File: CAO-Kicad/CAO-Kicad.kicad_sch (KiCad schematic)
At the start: 3 parts, among them J1 Conn_01x02

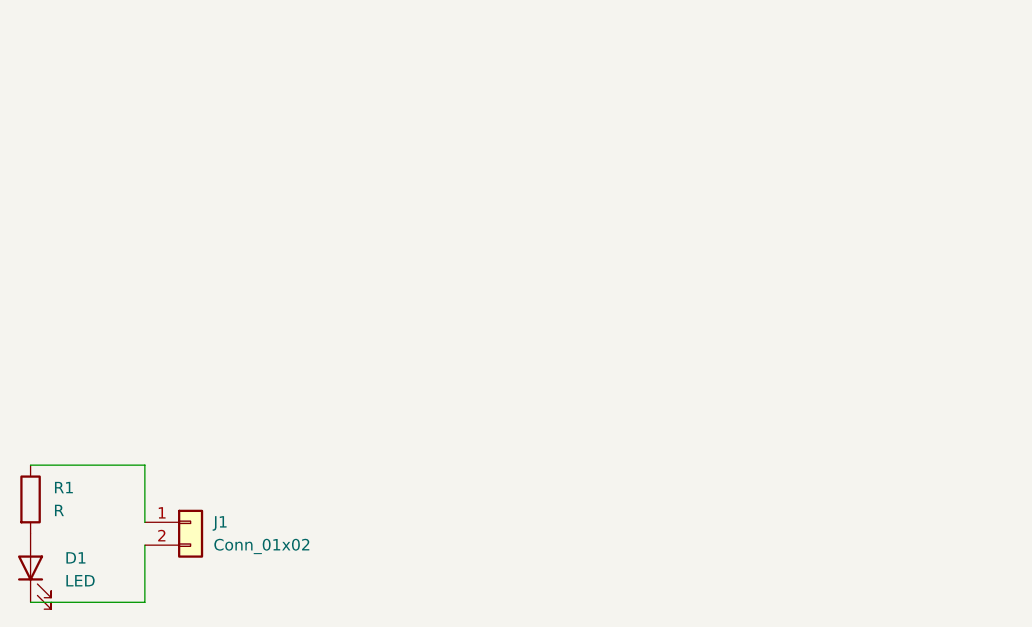
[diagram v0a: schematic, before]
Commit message: Ajout du conn ICSP et du contour de carte 100x100mm
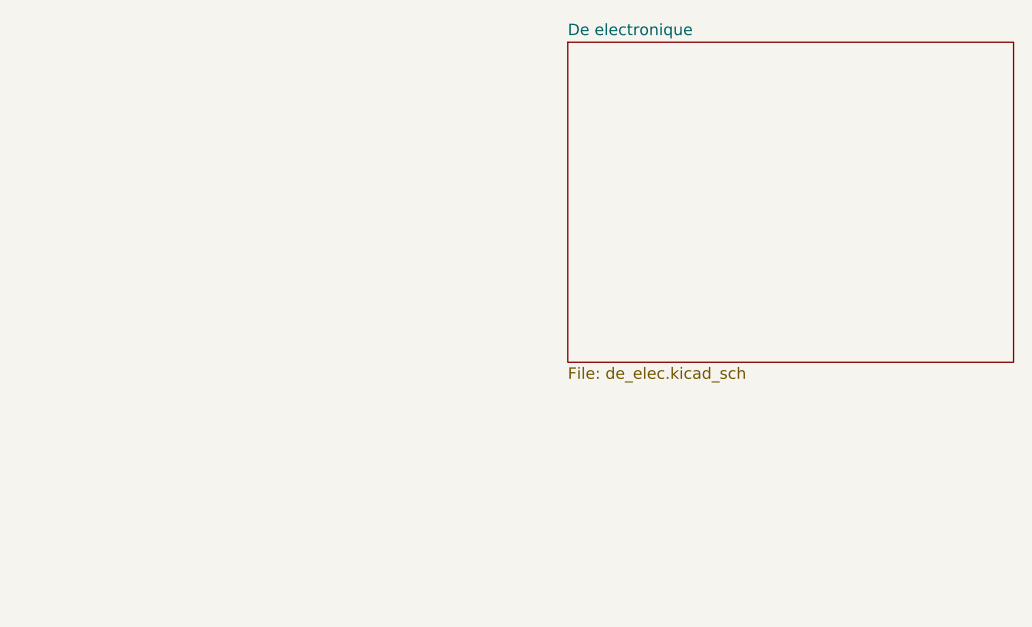
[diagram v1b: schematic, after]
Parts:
- removed D1: LED, LED_THT:LED_D5.0mm, symbol Device:LED
- removed J1: Conn_01x02, Connector_PinHeader_2.54mm:PinHeader_1x02_P2.54mm_Vertical, symbol Connector_Generic:Conn_01x02
- removed R1: R, Resistor_THT:R_Axial_DIN0207_L6.3mm_D2.5mm_P10.16mm_Horizontal, symbol Device:R
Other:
- added sheet De electronique (de_elec.kicad_sch)
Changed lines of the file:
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@@
     (rev "1.0")
   )
-  (wire (pts (xy 78.74 74.93) (xy 91.44 74.93))
-    (stroke (width 0) (type solid) (color 0 0 0 0))
-  )
-  (wire (pts (xy 78.74 90.17) (xy 91.44 90.17))
-    (stroke (width 0) (type solid) (color 0 0 0 0))
-  )
-  (wire (pts (xy 91.44 81.28) (xy 91.44 74.93))
-    (stroke (width 0) (type solid) (color 0 0 0 0))
-  )
-  (wire (pts (xy 91.44 83.82) (xy 91.44 90.17))
-    (stroke (width 0) (type solid) (color 0 0 0 0))
-  )
-  (symbol (lib_id "Device:R") (at 78.74 78.74 0) (unit 1)
-    (in_bom yes) (on_board yes) (fields_autoplaced)
-    (property "Reference" "R1" (id 0) (at 81.28 77.4699 0)
-      (effects (font (size 1.27 1.27)) (justify left))
+  (sheet (at 138.43 27.94) (size 49.53 35.56) (fields_autoplaced)
+    (stroke (width 0.0006) (type solid) (color 0 0 0 0))
+    (fill (color 0 0 0 0.0000))
+    (property "Nom feuille" "De electronique" (id 0) (at 138.43 27.3043 0)
+      (effects (font (size 1.27 1.27)) (justify left bottom))
     )
-    (property "Value" "R" (id 1) (at 81.28 80.0099 0)
-      (effects (font (size 1.27 1.27)) (justify left))
+    (property "Fichier de feuille" "de_elec.kicad_sch" (id 1) (at 138.43 64.0087 0)
+      (effects (font (size 1.27 1.27)) (justify left top))
     )
-    (property "Footprint" "Resistor_THT:R_Axial_DIN0207_L6.3mm_D2.5mm_P10.16mm_Horizontal" (id 2) (at 76.962 78.74 90)
-      (effects (font (size 1.27 1.27)) hide)
-    )
-    (property "Datasheet" "~" (id 3) (at 78.74 78.74 0)
-      (effects (font (size 1.27 1.27)) hide)
-    )
-    (pin "1")
-    (pin "2")
-  )
-  (symbol (lib_id "Device:LED") (at 78.74 86.36 90) (unit 1)
-    (in_bom yes) (on_board yes) (fields_autoplaced)
-    (property "Reference" "D1" (id 0) (at 82.55 85.2804 90)
-      (effects (font (size 1.27 1.27)) (justify right))
-    )
-    (property "Value" "LED" (id 1) (at 82.55 87.8204 90)
-      (effects (font (size 1.27 1.27)) (justify right))
-    )
-    (property "Footprint" "LED_THT:LED_D5.0mm" (id 2) (at 78.74 86.36 0)
-      (effects (font (size 1.27 1.27)) hide)
-    )
-    (property "Datasheet" "~" (id 3) (at 78.74 86.36 0)
-      (effects (font (size 1.27 1.27)) hide)
-    )
-    (pin "1")
-    (pin "2")
-  )
-  (symbol (lib_id "Connector_Generic:Conn_01x02") (at 96.52 81.28 0) (unit 1)
-    (in_bom yes) (on_board yes) (fields_autoplaced)
-    (property "Reference" "J1" (id 0) (at 99.06 81.2799 0)
-      (effects (font (size 1.27 1.27)) (justify left))
-    )
-    (property "Value" "Conn_01x02" (id 1) (at 99.06 83.8199 0)
-      (effects (font (size 1.27 1.27)) (justify left))
-    )
-    (property "Footprint" "Connector_PinHeader_2.54mm:PinHeader_1x02_P2.54mm_Vertical" (id 2) (at 96.52 81.28 0)
-      (effects (font (size 1.27 1.27)) hide)
-    )
-    (property "Datasheet" "~" (id 3) (at 96.52 81.28 0)
-      (effects (font (size 1.27 1.27)) hide)
-    )
-    (pin "1")
-    (pin "2")
   )
   (sheet_instances
     (path "/" (page "1"))
+    (path "/c75d577d-1368-4ac4-92ba-6ea9da14150f" (page "2"))
   )
   (symbol_instances
-    (path "/6f2e2640-7d35-4bbf-b1d2-20e69f68c07b"
-      (reference "D1") (unit 1) (value "LED") (footprint "LED_THT:LED_D5.0mm")
+    (path "/c75d577d-1368-4ac4-92ba-6ea9da14150f/3f12aa33-9c08-4a66-904f-7ff507ac6010"
+      (reference "D?") (unit 1) (value "LED") (footprint "LED_THT:LED_D5.0mm")
     )
-    (path "/79d0a340-8f69-4e94-8e4f-f98bc996c44d"
-      (reference "J1") (unit 1) (value "Conn_01x02") (footprint "Connector_PinHeader_2.54mm:PinHeader_1x02_P2.54mm_Vertical")
+    (path "/c75d577d-1368-4ac4-92ba-6ea9da14150f/44f833d5-7c87-4378-a885-fbac1347757e"
+      (reference "D?") (unit 1) (value "LED") (footprint "LED_THT:LED_D5.0mm")
     )
-    (path "/3bf84ff4-4546-454c-aed1-77b48fa86e13"
-      (reference "R1") (unit 1) (value "R") (footprint "Resistor_THT:R_Axial_DIN0207_L6.3mm_D2.5mm_P10.16mm_Horizontal")
+    (path "/c75d577d-1368-4ac4-92ba-6ea9da14150f/4f063d99-02c1-4629-8d36-12c6ac14329c"
+      (reference "D?") (unit 1) (value "LED") (footprint "LED_THT:LED_D5.0mm")
+    )
+    (path "/c75d577d-1368-4ac4-92ba-6ea9da14150f/4266caad-59c2-4e8d-9eec-bfc208f99b2e"
+      (reference "J?") (unit 1) (value "Conn_01x02") (footprint "Connector_PinHeader_2.54mm:PinHeader_1x02_P2.54mm_Vertical")
+    )
+    (path "/c75d577d-1368-4ac4-92ba-6ea9da14150f/32a5e041-8201-47e0-ada2-733638341093"
+      (reference "R?") (unit 1) (value "R") (footprint "Resistor_THT:R_Axial_DIN0207_L6.3mm_D2.5mm_P10.16mm_Horizontal")
+    )
+    (path "/c75d577d-1368-4ac4-92ba-6ea9da14150f/9f2305e5-4fff-4a3e-8010-f82c5e257aa7"
+      (reference "R?") (unit 1) (value "R") (footprint "Resistor_THT:R_Axial_DIN0207_L6.3mm_D2.5mm_P10.16mm_Horizontal")
+    )
+    (path "/c75d577d-1368-4ac4-92ba-6ea9da14150f/fa47fbcc-6406-45c3-a820-b36f7819cbc6"
+      (reference "R?") (unit 1) (value "R") (footprint "Resistor_THT:R_Axial_DIN0207_L6.3mm_D2.5mm_P10.16mm_Horizontal")
     )
   )

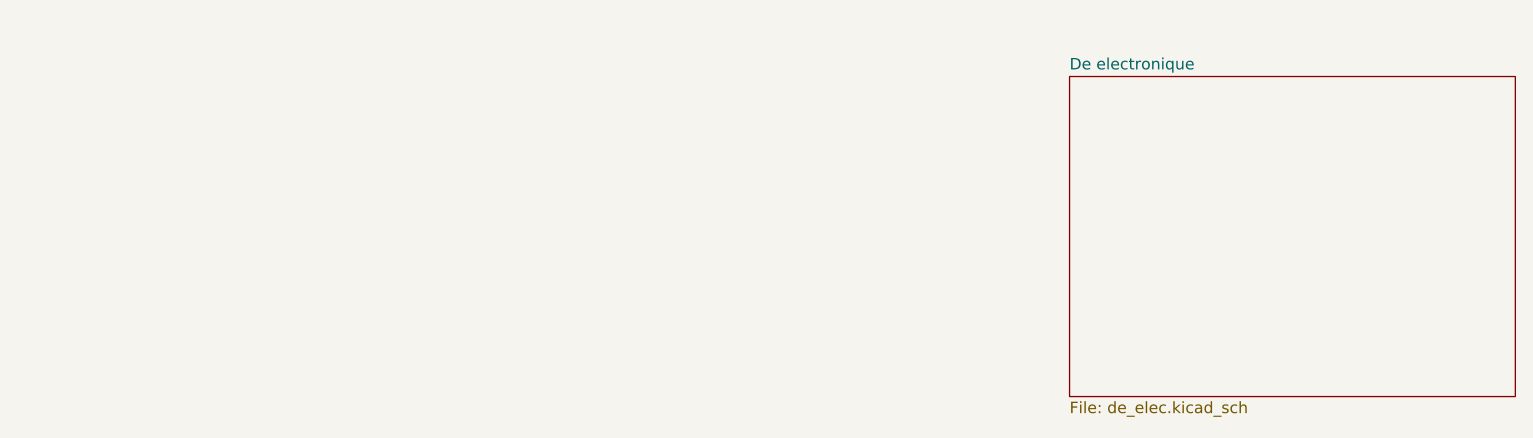
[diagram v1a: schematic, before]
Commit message: Ajout de la serigraphie et recherche composants
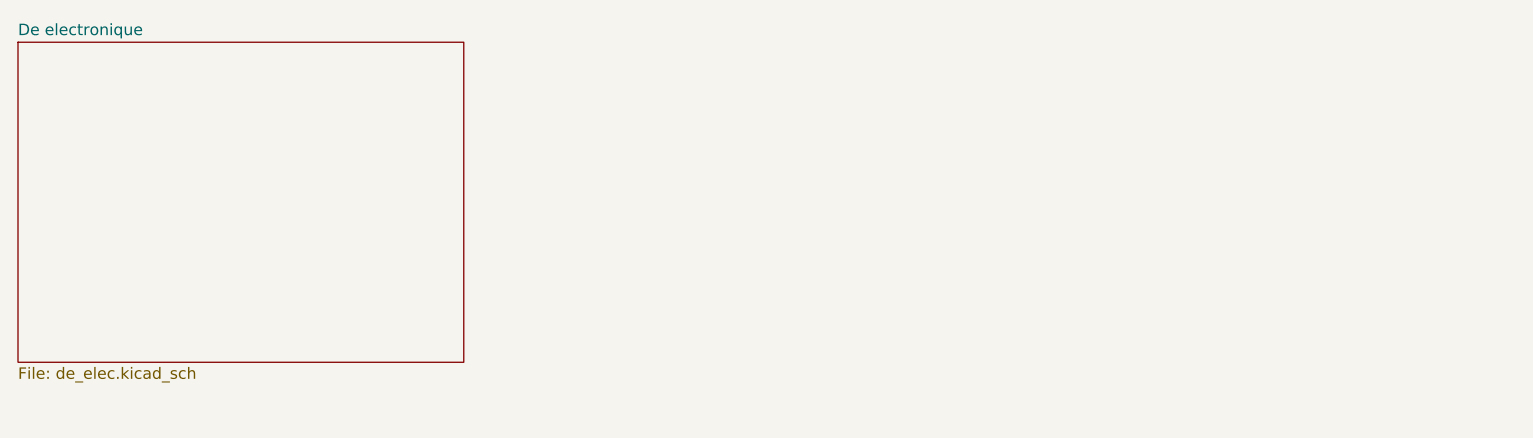
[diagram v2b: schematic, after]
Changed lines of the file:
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@@
     (rev "1.0")
   )
-  (sheet (at 138.43 27.94) (size 49.53 35.56) (fields_autoplaced)
+  (sheet (at 21.59 24.13) (size 49.53 35.56) (fields_autoplaced)
     (stroke (width 0.0006) (type solid) (color 0 0 0 0))
     (fill (color 0 0 0 0.0000))
-    (property "Nom feuille" "De electronique" (id 0) (at 138.43 27.3043 0)
+    (property "Nom feuille" "De electronique" (id 0) (at 21.59 23.4943 0)
       (effects (font (size 1.27 1.27)) (justify left bottom))
     )
-    (property "Fichier de feuille" "de_elec.kicad_sch" (id 1) (at 138.43 64.0087 0)
+    (property "Fichier de feuille" "de_elec.kicad_sch" (id 1) (at 21.59 60.1987 0)
       (effects (font (size 1.27 1.27)) (justify left top))
     )
@@
   )
   (symbol_instances
-    (path "/c75d577d-1368-4ac4-92ba-6ea9da14150f/3f12aa33-9c08-4a66-904f-7ff507ac6010"
-      (reference "D?") (unit 1) (value "LED") (footprint "LED_THT:LED_D5.0mm")
+    (path "/c75d577d-1368-4ac4-92ba-6ea9da14150f/c856c994-3b28-46d2-b6c4-cfd4a09bdf0c"
+      (reference "#PWR01") (unit 1) (value "VCC") (footprint "")
     )
-    (path "/c75d577d-1368-4ac4-92ba-6ea9da14150f/44f833d5-7c87-4378-a885-fbac1347757e"
-      (reference "D?") (unit 1) (value "LED") (footprint "LED_THT:LED_D5.0mm")
+    (path "/c75d577d-1368-4ac4-92ba-6ea9da14150f/1998137d-0916-4d35-b6a8-e92d9d88d9dc"
+      (reference "#PWR02") (unit 1) (value "GND") (footprint "")
     )
-    (path "/c75d577d-1368-4ac4-92ba-6ea9da14150f/4f063d99-02c1-4629-8d36-12c6ac14329c"
-      (reference "D?") (unit 1) (value "LED") (footprint "LED_THT:LED_D5.0mm")
+    (path "/c75d577d-1368-4ac4-92ba-6ea9da14150f/52cf1731-350f-4222-bdcf-436321ebfe1f"
+      (reference "#PWR03") (unit 1) (value "GND") (footprint "")
     )
-    (path "/c75d577d-1368-4ac4-92ba-6ea9da14150f/4266caad-59c2-4e8d-9eec-bfc208f99b2e"
-      (reference "J?") (unit 1) (value "Conn_01x02") (footprint "Connector_PinHeader_2.54mm:PinHeader_1x02_P2.54mm_Vertical")
+    (path "/c75d577d-1368-4ac4-92ba-6ea9da14150f/df5405e6-7309-4ce9-9d02-d2d52ba65d7a"
+      (reference "#PWR04") (unit 1) (value "GND") (footprint "")
     )
-    (path "/c75d577d-1368-4ac4-92ba-6ea9da14150f/32a5e041-8201-47e0-ada2-733638341093"
-      (reference "R?") (unit 1) (value "R") (footprint "Resistor_THT:R_Axial_DIN0207_L6.3mm_D2.5mm_P10.16mm_Horizontal")
+    (path "/c75d577d-1368-4ac4-92ba-6ea9da14150f/920ad638-99a8-4d76-835e-97f6426f6f3f"
+      (reference "#PWR05") (unit 1) (value "VCC") (footprint "")
     )
-    (path "/c75d577d-1368-4ac4-92ba-6ea9da14150f/9f2305e5-4fff-4a3e-8010-f82c5e257aa7"
-      (reference "R?") (unit 1) (value "R") (footprint "Resistor_THT:R_Axial_DIN0207_L6.3mm_D2.5mm_P10.16mm_Horizontal")
+    (path "/c75d577d-1368-4ac4-92ba-6ea9da14150f/688d37b9-5a58-45b4-8009-efbd093e7f76"
+      (reference "#PWR06") (unit 1) (value "GND") (footprint "")
     )
-    (path "/c75d577d-1368-4ac4-92ba-6ea9da14150f/fa47fbcc-6406-45c3-a820-b36f7819cbc6"
-      (reference "R?") (unit 1) (value "R") (footprint "Resistor_THT:R_Axial_DIN0207_L6.3mm_D2.5mm_P10.16mm_Horizontal")
+    (path "/c75d577d-1368-4ac4-92ba-6ea9da14150f/72356204-2236-4316-9251-37eeb9ae35a9"
+      (reference "C1") (unit 1) (value "C") (footprint "")
+    )
+    (path "/c75d577d-1368-4ac4-92ba-6ea9da14150f/2c513e4b-3ebb-4785-9087-8281c413a06a"
+      (reference "C2") (unit 1) (value "C_Polarized") (footprint "")
+    )
+    (path "/c75d577d-1368-4ac4-92ba-6ea9da14150f/bb6949a4-bc90-4481-a7dc-0ea01082aa6f"
+      (reference "D1") (unit 1) (value "LED") (footprint "LEDs:LED_D5.0mm")
+    )
+    (path "/c75d577d-1368-4ac4-92ba-6ea9da14150f/fe946614-6461-492a-a691-f496e1f6fd7a"
+      (reference "D2") (unit 1) (value "LED") (footprint "LEDs:LED_D5.0mm")
+    )
+    (path "/c75d577d-1368-4ac4-92ba-6ea9da14150f/7a824bb0-27de-44cc-9aef-e67f76c0731f"
+      (reference "D3") (unit 1) (value "LED") (footprint "LEDs:LED_D5.0mm")
+    )
+    (path "/c75d577d-1368-4ac4-92ba-6ea9da14150f/d8b5cf32-7977-462a-bd9e-42c5f4188d00"
+      (reference "D4") (unit 1) (value "LED") (footprint "LEDs:LED_D5.0mm")
+    )
+    (path "/c75d577d-1368-4ac4-92ba-6ea9da14150f/fc573955-b38f-4418-a1a4-a0648d45394b"
+      (reference "D5") (unit 1) (value "LED") (footprint "LEDs:LED_D5.0mm")
+    )
+    (path "/c75d577d-1368-4ac4-92ba-6ea9da14150f/3527e604-fe69-4b72-98b7-22c7a91f656c"
+      (reference "D6") (unit 1) (value "LED") (footprint "LEDs:LED_D5.0mm")
+    )
+    (path "/c75d577d-1368-4ac4-92ba-6ea9da14150f/15355201-f677-4b9e-809e-c66c0865243d"
+      (reference "D7") (unit 1) (value "LED") (footprint "LEDs:LED_D5.0mm")
+    )
+    (path "/c75d577d-1368-4ac4-92ba-6ea9da14150f/86ee8edf-b2e8-48a8-8002-16f4ddfd214a"
+      (reference "J1") (unit 1) (value "ICSP") (footprint "")
+    )
+    (path "/c75d577d-1368-4ac4-92ba-6ea9da14150f/d1e8852a-36a2-4017-bd90-ce0b4a9fd52d"
+      (reference "JP1") (unit 1) (value "Jumper_2_Open") (footprint "")
+    )
+    (path "/c75d577d-1368-4ac4-92ba-6ea9da14150f/f1f8c76a-4611-4569-9196-e9181ae3985a"
+      (reference "R1") (unit 1) (value "1k") (footprint "Resistors_SMD:R_0805_HandSoldering")
+    )
+    (path "/c75d577d-1368-4ac4-92ba-6ea9da14150f/668a947c-dd02-4a5f-8d8e-c0723fae0c49"
+      (reference "R2") (unit 1) (value "560") (footprint "Resistors_SMD:R_0805_HandSoldering")
+    )
+    (path "/c75d577d-1368-4ac4-92ba-6ea9da14150f/aad576ff-1a2a-4904-9f6a-e7de31a63638"
+      (reference "R3") (unit 1) (value "560") (footprint "Resistors_SMD:R_0805_HandSoldering")
+    )
+    (path "/c75d577d-1368-4ac4-92ba-6ea9da14150f/8c03dd69-34d3-4aa4-afcd-a6b9bd57fd13"
+      (reference "R4") (unit 1) (value "560") (footprint "Resistors_SMD:R_0805_HandSoldering")
+    )
+    (path "/c75d577d-1368-4ac4-92ba-6ea9da14150f/9efa6f65-5d79-4e30-896b-d1238995c3ba"
+      (reference "SW1") (unit 1) (value "COMMUTATEUR VIBRATION") (footprint "Capacitors_THT:CP_Radial_D5.0mm_P2.50mm")
+    )
+    (path "/c75d577d-1368-4ac4-92ba-6ea9da14150f/c456604f-e26f-4f54-816c-9e3874bc3628"
+      (reference "U1") (unit 1) (value "puce de microcontrôleur IC ATTINY85 MCU 8BIT ATTINY 20MHZ, 8 broches DIP-8") (footprint "Housings_DIP:DIP-8_W7.62mm")
     )
   )
